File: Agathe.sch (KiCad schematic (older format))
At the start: 173 parts, among them J1 Conn_01x04_Female, J2 GPIO 1, J3 GPIO 2, J4 Conn_01x02_Female, SW1 SW_Push, U1 ATmega32U4-AU, U2 PRTR5V0U2X, Y1 Crystal_GND24_Small

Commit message: add value for rst resistor and crystal (#2)
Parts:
- R4: value R_Small -> 10k
- Y1: value Crystal_GND24_Small -> 16MHz
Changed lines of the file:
@@
 P 3950 7150
 F 0 "Y1" V 3904 7294 50  0000 L CNN
-F 1 "Crystal_GND24_Small" V 3995 7294 50  0000 L CNN
+F 1 "16MHz" V 3995 7294 50  0000 L CNN
 F 2 "Crystal:Crystal_SMD_3225-4Pin_3.2x2.5mm" H 3950 7150 50  0001 C CNN
 F 3 "~" H 3950 7150 50  0001 C CNN
@@
 P 1350 900
 F 0 "R4" H 1409 946 50  0000 L CNN
-F 1 "R_Small" H 1409 855 50  0000 L CNN
+F 1 "10k" H 1409 855 50  0000 L CNN
 F 2 "Resistor_SMD:R_0805_2012Metric" H 1350 900 50  0001 C CNN
 F 3 "~" H 1350 900 50  0001 C CNN

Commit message: Move J2 to top
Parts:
- removed J2: GPIO 1, Connector_PinHeader_2.54mm:PinHeader_1x01_P2.54mm_Vertical, symbol Connector:Conn_01x01_Female
- removed J3: GPIO 2, Connector_PinHeader_2.54mm:PinHeader_1x01_P2.54mm_Vertical, symbol Connector:Conn_01x01_Female
- added J2: Conn_01x02_Female, Connector_PinHeader_2.54mm:PinHeader_1x02_P2.54mm_Vertical, symbol Connector:Conn_01x02_Female
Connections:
- net labels added: GPIO1, GPIO2
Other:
- moved on the sheet: J4
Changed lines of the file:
@@
 Connection ~ 10000 3200
-$Comp
-L MCU_Microchip_ATmega:ATmega32U4-AU U1
-U 1 1 5EC4E28C
-P 1950 2700
-F 0 "U1" H 1950 811 50  0000 C CNN
-F 1 "ATmega32U4-AU" H 1950 720 50  0000 C CNN
-F 2 "Keebio-Parts:ATMEGA32U4-AU" H 1950 2700 50  0001 C CIN
-F 3 "http://ww1.microchip.com/downloads/en/DeviceDoc/Atmel-7766-8-bit-AVR-ATmega16U4-32U4_Datasheet.pdf" H 1950 2700 50  0001 C CNN
-	1    1950 2700
-	1    0    0    -1
-$EndComp
 $Comp
 L power:GND #PWR0101
@@
 Wire Wire Line
 	1950 4500 1850 4500
-Connection ~ 1950 4500
 $Comp
 L power:+5V #PWR0102
@@
 Wire Wire Line
 	1850 700  1850 900
-Wire Wire Line
-	1850 900  1950 900
-Connection ~ 1850 900
-Connection ~ 1950 900
-Wire Wire Line
-	1950 900  2050 900
 $Comp
 L Device:R_Small R1
@@
 Wire Wire Line
 	1350 1000 1350 1200
-Connection ~ 1350 1200
 $Comp
 L power:+5V #PWR0110
@@
 Text GLabel 2550 2400 2    50   Input ~ 0
 COL13
-Wire Wire Line
-	2550 3300 2900 3300
 Text GLabel 2550 2500 2    50   Input ~ 0
 COL12
@@
 $EndComp
 $Comp
-L Connector:Conn_01x01_Female J2
-U 1 1 5F7E232B
-P 2750 3400
-F 0 "J2" H 2778 3426 50  0000 L CNN
-F 1 "GPIO 1" H 2778 3335 50  0000 L CNN
-F 2 "Connector_PinHeader_2.54mm:PinHeader_1x01_P2.54mm_Vertical" H 2750 3400 50  0001 C CNN
-F 3 "~" H 2750 3400 50  0001 C CNN
-	1    2750 3400
-	1    0    0    -1
-$EndComp
-$Comp
-L Connector:Conn_01x01_Female J3
-U 1 1 5F7E3E80
-P 2750 4000
-F 0 "J3" H 2778 4026 50  0000 L CNN
-F 1 "GPIO 2" H 2778 3935 50  0000 L CNN
-F 2 "Connector_PinHeader_2.54mm:PinHeader_1x01_P2.54mm_Vertical" H 2750 4000 50  0001 C CNN
-F 3 "~" H 2750 4000 50  0001 C CNN
-	1    2750 4000
-	1    0    0    -1
-$EndComp
-$Comp
 L Connector:Conn_01x02_Female J4
 U 1 1 5F803717
-P 4850 6600
-F 0 "J4" H 4878 6576 50  0000 L CNN
-F 1 "Conn_01x02_Female" H 4878 6485 50  0000 L CNN
-F 2 "Connector_PinHeader_2.54mm:PinHeader_1x02_P2.54mm_Vertical" H 4850 6600 50  0001 C CNN
-F 3 "~" H 4850 6600 50  0001 C CNN
-	1    4850 6600
+P 5200 6450
+F 0 "J4" H 5228 6426 50  0000 L CNN
+F 1 "Conn_01x02_Female" H 5228 6335 50  0000 L CNN
+F 2 "Connector_PinHeader_2.54mm:PinHeader_1x02_P2.54mm_Vertical" H 5200 6450 50  0001 C CNN
+F 3 "~" H 5200 6450 50  0001 C CNN
+	1    5200 6450
 	1    0    0    -1
 $EndComp
@@
 L power:VCC #PWR03
 U 1 1 5F805F11
-P 4650 6600
-F 0 "#PWR03" H 4650 6450 50  0001 C CNN
-F 1 "VCC" H 4665 6773 50  0000 C CNN
-F 2 "" H 4650 6600 50  0001 C CNN
-F 3 "" H 4650 6600 50  0001 C CNN
-	1    4650 6600
+P 5000 6450
+F 0 "#PWR03" H 5000 6300 50  0001 C CNN
+F 1 "VCC" H 5015 6623 50  0000 C CNN
+F 2 "" H 5000 6450 50  0001 C CNN
+F 3 "" H 5000 6450 50  0001 C CNN
+	1    5000 6450
 	1    0    0    -1
 $EndComp
@@
 L power:GND #PWR04
 U 1 1 5F807ABA
-P 4650 6700
-F 0 "#PWR04" H 4650 6450 50  0001 C CNN
-F 1 "GND" H 4655 6527 50  0000 C CNN
-F 2 "" H 4650 6700 50  0001 C CNN
-F 3 "" H 4650 6700 50  0001 C CNN
-	1    4650 6700
-	1    0    0    -1
-$EndComp
+P 5000 6550
+F 0 "#PWR04" H 5000 6300 50  0001 C CNN
+F 1 "GND" H 5005 6377 50  0000 C CNN
+F 2 "" H 5000 6550 50  0001 C CNN
+F 3 "" H 5000 6550 50  0001 C CNN
+	1    5000 6550
+	1    0    0    -1
+$EndComp
+$Comp
+L Connector:Conn_01x02_Female J2
+U 1 1 5F858F30
+P 5150 7150
+F 0 "J2" H 5178 7126 50  0000 L CNN
+F 1 "Conn_01x02_Female" H 5178 7035 50  0000 L CNN
+F 2 "Connector_PinHeader_2.54mm:PinHeader_1x02_P2.54mm_Vertical" H 5150 7150 50  0001 C CNN
+F 3 "~" H 5150 7150 50  0001 C CNN
+	1    5150 7150
+	1    0    0    -1
+$EndComp
+Text GLabel 2550 4000 2    50   Input ~ 0
+GPIO2
+Connection ~ 1350 1200
+Connection ~ 1950 900
+Connection ~ 1850 900
+Wire Wire Line
+	1850 900  1950 900
+Connection ~ 1950 4500
+Wire Wire Line
+	2550 3300 2900 3300
+Wire Wire Line
+	1950 900  2050 900
+Text GLabel 2550 3400 2    50   Input ~ 0
+GPIO1
+$Comp
+L MCU_Microchip_ATmega:ATmega32U4-AU U1
+U 1 1 5EC4E28C
+P 1950 2700
+F 0 "U1" H 1950 811 50  0000 C CNN
+F 1 "ATmega32U4-AU" H 1950 720 50  0000 C CNN
+F 2 "Keebio-Parts:ATMEGA32U4-AU" H 1950 2700 50  0001 C CIN
+F 3 "http://ww1.microchip.com/downloads/en/DeviceDoc/Atmel-7766-8-bit-AVR-ATmega16U4-32U4_Datasheet.pdf" H 1950 2700 50  0001 C CNN
+	1    1950 2700
+	1    0    0    -1
+$EndComp
+Text GLabel 4950 7150 0    50   Input ~ 0
+GPIO1
+Text GLabel 4950 7250 0    50   Input ~ 0
+GPIO2
 $EndSCHEMATC

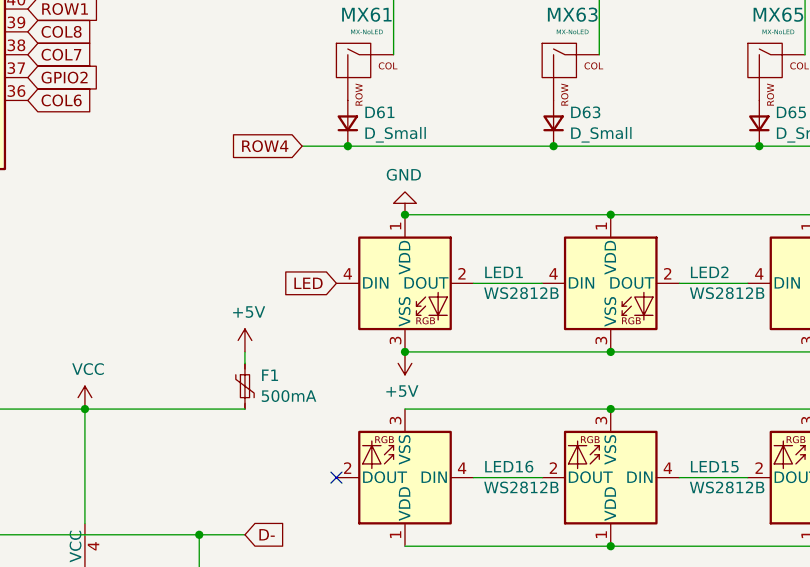
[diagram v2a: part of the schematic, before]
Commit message: reverse vcc and gnd on leds (#9)
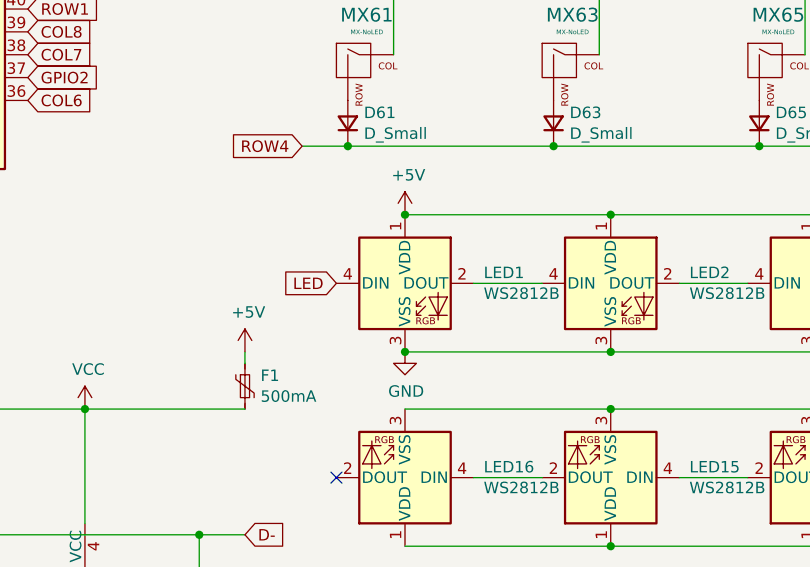
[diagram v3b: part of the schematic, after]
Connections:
- net +5V: now also LED1.1 (VDD), LED10.1 (VDD), LED11.1 (VDD), LED12.1 (VDD), LED13.1 (VDD), LED14.1 (VDD), LED15.1 (VDD), LED16.1 (VDD), LED2.1 (VDD), LED3.1 (VDD), LED4.1 (VDD), LED5.1 (VDD), LED6.1 (VDD), LED7.1 (VDD), LED8.1 (VDD), LED9.1 (VDD); no longer LED1.3 (VSS), LED10.3 (VSS), LED11.3 (VSS), LED12.3 (VSS), LED13.3 (VSS), LED14.3 (VSS), LED15.3 (VSS), LED16.3 (VSS), LED2.3 (VSS), LED3.3 (VSS), LED4.3 (VSS), LED5.3 (VSS), LED6.3 (VSS), LED7.3 (VSS), LED8.3 (VSS), LED9.3 (VSS)
- net GND: now also LED1.3 (VSS), LED10.3 (VSS), LED11.3 (VSS), LED12.3 (VSS), LED13.3 (VSS), LED14.3 (VSS), LED15.3 (VSS), LED16.3 (VSS), LED2.3 (VSS), LED3.3 (VSS), LED4.3 (VSS), LED5.3 (VSS), LED6.3 (VSS), LED7.3 (VSS), LED8.3 (VSS), LED9.3 (VSS); no longer LED1.1 (VDD), LED10.1 (VDD), LED11.1 (VDD), LED12.1 (VDD), LED13.1 (VDD), LED14.1 (VDD), LED15.1 (VDD), LED16.1 (VDD), LED2.1 (VDD), LED3.1 (VDD), LED4.1 (VDD), LED5.1 (VDD), LED6.1 (VDD), LED7.1 (VDD), LED8.1 (VDD), LED9.1 (VDD)
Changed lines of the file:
@@
 L power:GND #PWR0117
 U 1 1 5EE29498
-P 4200 4600
-F 0 "#PWR0117" H 4200 4350 50  0001 C CNN
-F 1 "GND" H 4205 4427 50  0000 C CNN
-F 2 "" H 4200 4600 50  0001 C CNN
-F 3 "" H 4200 4600 50  0001 C CNN
-	1    4200 4600
-	-1   0    0    1
+P 4200 5200
+F 0 "#PWR0117" H 4200 4950 50  0001 C CNN
+F 1 "GND" H 4205 5027 50  0000 C CNN
+F 2 "" H 4200 5200 50  0001 C CNN
+F 3 "" H 4200 5200 50  0001 C CNN
+	1    4200 5200
+	1    0    0    -1
 $EndComp
 Text GLabel 3900 4900 0    50   Input ~ 0
@@
 L power:+5V #PWR0118
 U 1 1 5F100FF1
-P 4200 5200
-F 0 "#PWR0118" H 4200 5050 50  0001 C CNN
-F 1 "+5V" H 4215 5373 50  0000 C CNN
-F 2 "" H 4200 5200 50  0001 C CNN
-F 3 "" H 4200 5200 50  0001 C CNN
-	1    4200 5200
-	-1   0    0    1
+P 4200 4600
+F 0 "#PWR0118" H 4200 4450 50  0001 C CNN
+F 1 "+5V" H 4215 4773 50  0000 C CNN
+F 2 "" H 4200 4600 50  0001 C CNN
+F 3 "" H 4200 4600 50  0001 C CNN
+	1    4200 4600
+	1    0    0    -1
 $EndComp
 Connection ~ 4200 5200

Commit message: add a capacitor
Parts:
- added C8: 0.1uF, Capacitor_SMD:C_0805_2012Metric, symbol Device:C_Small
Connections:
- net +5V: now also C8.1
- net GND: now also C8.2
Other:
- moved on the sheet: C5
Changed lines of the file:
@@
 L Device:C_Small C5
 U 1 1 5ED00BF8
-P 1800 7450
-F 0 "C5" H 1892 7496 50  0000 L CNN
-F 1 "10uF" H 1892 7405 50  0000 L CNN
-F 2 "Capacitor_SMD:C_0805_2012Metric" H 1800 7450 50  0001 C CNN
-F 3 "~" H 1800 7450 50  0001 C CNN
-	1    1800 7450
+P 2200 7450
+F 0 "C5" H 2292 7496 50  0000 L CNN
+F 1 "10uF" H 2292 7405 50  0000 L CNN
+F 2 "Capacitor_SMD:C_0805_2012Metric" H 2200 7450 50  0001 C CNN
+F 3 "~" H 2200 7450 50  0001 C CNN
+	1    2200 7450
 	1    0    0    -1
 $EndComp
@@
 L power:+5V #PWR0105
 U 1 1 5ED02584
-P 1250 7350
-F 0 "#PWR0105" H 1250 7200 50  0001 C CNN
-F 1 "+5V" H 1265 7523 50  0000 C CNN
-F 2 "" H 1250 7350 50  0001 C CNN
-F 3 "" H 1250 7350 50  0001 C CNN
-	1    1250 7350
+P 1400 7350
+F 0 "#PWR0105" H 1400 7200 50  0001 C CNN
+F 1 "+5V" H 1415 7523 50  0000 C CNN
+F 2 "" H 1400 7350 50  0001 C CNN
+F 3 "" H 1400 7350 50  0001 C CNN
+	1    1400 7350
 	1    0    0    -1
 $EndComp
@@
 L power:GND #PWR0106
 U 1 1 5ED03888
-P 1250 7550
-F 0 "#PWR0106" H 1250 7300 50  0001 C CNN
-F 1 "GND" H 1255 7377 50  0000 C CNN
-F 2 "" H 1250 7550 50  0001 C CNN
-F 3 "" H 1250 7550 50  0001 C CNN
-	1    1250 7550
-	1    0    0    -1
-$EndComp
-Connection ~ 1250 7550
-Wire Wire Line
-	1800 7350 1400 7350
+P 1400 7550
+F 0 "#PWR0106" H 1400 7300 50  0001 C CNN
+F 1 "GND" H 1405 7377 50  0000 C CNN
+F 2 "" H 1400 7550 50  0001 C CNN
+F 3 "" H 1400 7550 50  0001 C CNN
+	1    1400 7550
+	1    0    0    -1
+$EndComp
 Connection ~ 1000 7350
 Wire Wire Line
 	1000 7350 600  7350
-Connection ~ 1250 7350
-Wire Wire Line
-	1250 7350 1000 7350
 Connection ~ 1400 7350
-Wire Wire Line
-	1400 7350 1250 7350
 $Comp
 L power:+5V #PWR0107
@@
 Wire Wire Line
 	600  7550 1000 7550
-Wire Wire Line
-	1250 7550 1400 7550
 Connection ~ 1000 7550
-Wire Wire Line
-	1000 7550 1250 7550
 Connection ~ 1400 7550
-Wire Wire Line
-	1400 7550 1800 7550
 NoConn ~ 1550 6550
 Wire Wire Line
@@
 Text GLabel 4950 7250 0    50   Input ~ 0
 GPIO2
+$Comp
+L Device:C_Small C8
+U 1 1 5F97460A
+P 1800 7450
+F 0 "C8" H 1892 7496 50  0000 L CNN
+F 1 "0.1uF" H 1892 7405 50  0000 L CNN
+F 2 "Capacitor_SMD:C_0805_2012Metric" H 1800 7450 50  0001 C CNN
+F 3 "~" H 1800 7450 50  0001 C CNN
+	1    1800 7450
+	1    0    0    -1
+$EndComp
+Wire Wire Line
+	1400 7350 1800 7350
+Wire Wire Line
+	1400 7550 1800 7550
+Wire Wire Line
+	1800 7550 2200 7550
+Connection ~ 1800 7550
+Wire Wire Line
+	1800 7350 2200 7350
+Connection ~ 1800 7350
+Wire Wire Line
+	1000 7550 1400 7550
+Wire Wire Line
+	1000 7350 1400 7350
 $EndSCHEMATC

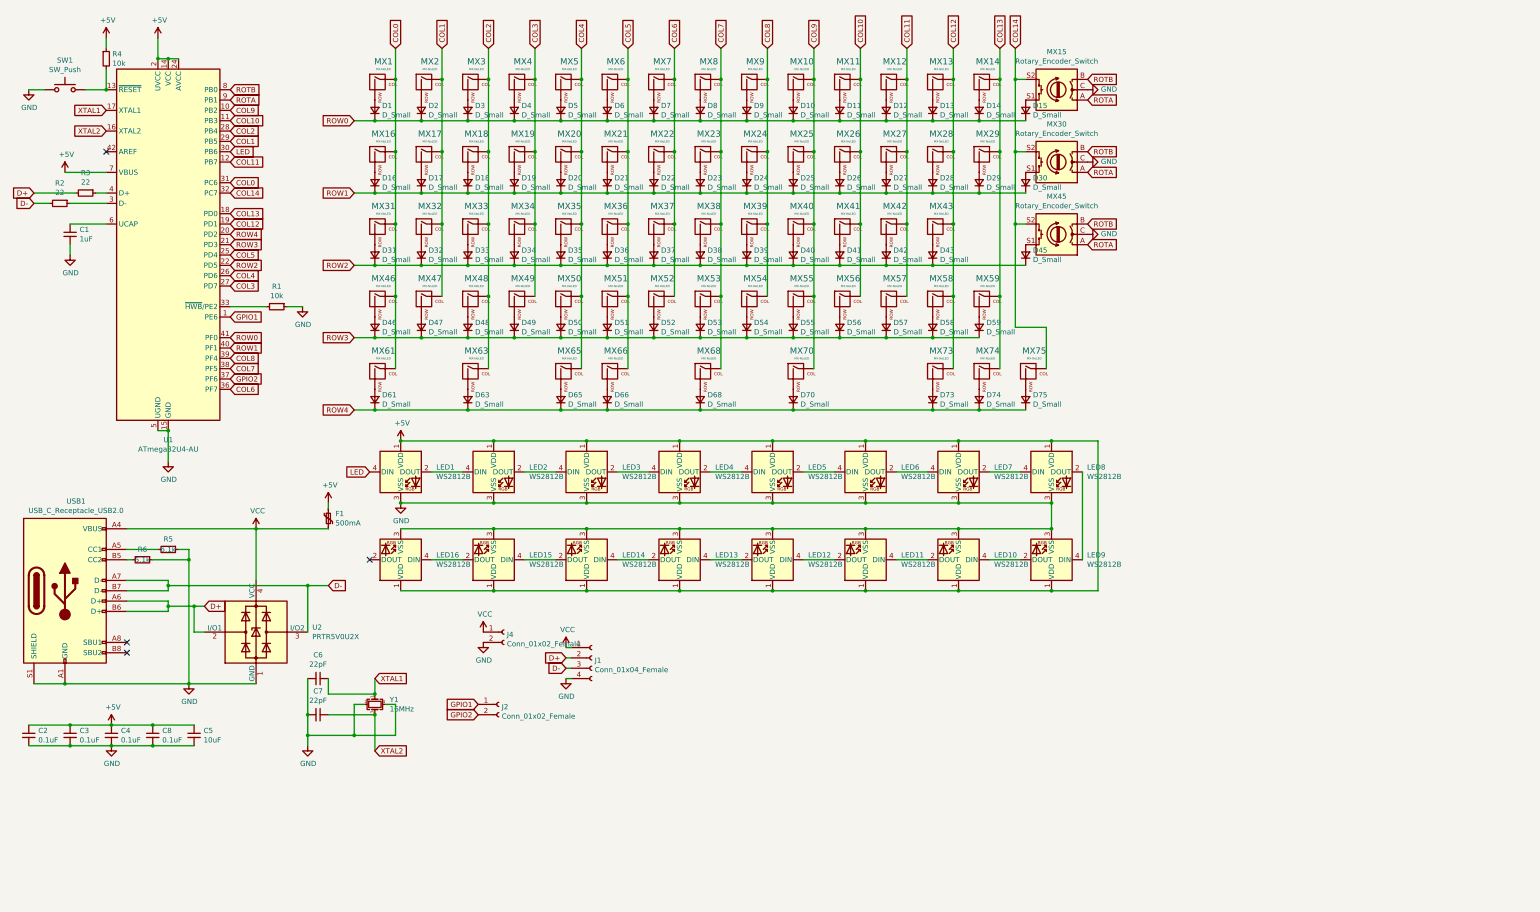
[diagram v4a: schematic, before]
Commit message: update shematics
add spi interface
add 6 leds
change the esp
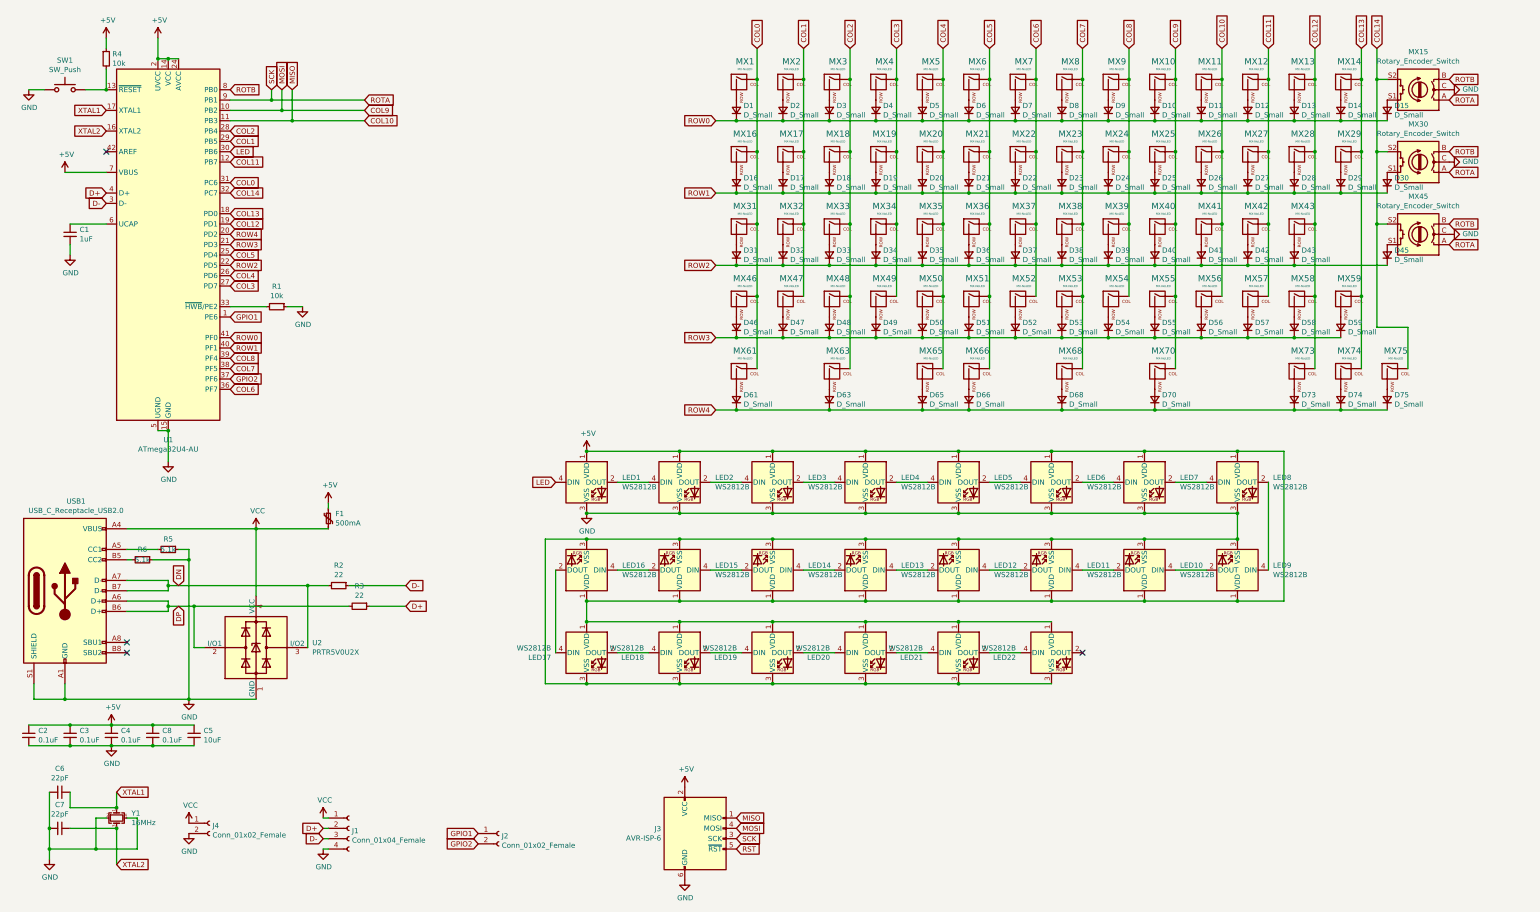
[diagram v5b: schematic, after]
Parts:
- added J3: AVR-ISP-6, random-keyboard-parts:Reset_Pretty-Mask, symbol Connector:AVR-ISP-6
- added LED17, LED18, LED19, LED20, LED21, LED22: WS2812B, LED_SMD:LED_WS2812B_PLCC4_5.0x5.0mm_P3.2mm, symbol LED:WS2812B
- U2: footprint Package_TO_SOT_SMD:SOT-143 -> random-keyboard-parts:SOT143B
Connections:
- net +5V: now also J3.2 (VCC), LED17.1 (VDD), LED18.1 (VDD), LED19.1 (VDD), LED20.1 (VDD), LED21.1 (VDD), LED22.1 (VDD)
- net COL10: now also J3.1 (MISO)
- net COL9: now also J3.4 (MOSI)
- net D+: now also R3.1, U1.4 (D+); no longer R3.2, U2.2 (I/O1), USB1.A6 (D+), USB1.B6 (D+)
- net D-: now also R2.1, U1.3 (D-); no longer R2.2, U2.3 (I/O2), USB1.A7 (D-), USB1.B7 (D-)
- net GND: now also J3.6 (GND), LED17.3 (VSS), LED18.3 (VSS), LED19.3 (VSS), LED20.3 (VSS), LED21.3 (VSS), LED22.3 (VSS)
- net ROTA: now also J3.3 (SCK)
- net at LED16.2 (DOUT): now also LED17.4 (DIN)
- new net: LED17.2 (DOUT), LED18.4 (DIN)
- new net: LED18.2 (DOUT), LED19.4 (DIN)
- new net: LED19.2 (DOUT), LED20.4 (DIN)
- new net: LED20.2 (DOUT), LED21.4 (DIN)
- new net: LED21.2 (DOUT), LED22.4 (DIN)
- new net DN: R2.2, U2.3 (I/O2), USB1.A7 (D-), USB1.B7 (D-)
- new net DP: R3.2, U2.2 (I/O1), USB1.A6 (D+), USB1.B6 (D+)
- new net RST: J3.5 (~RST)
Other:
- moved on the sheet: C6, C7, D1, D10, D11, D12, D13, D14, D15, D16, D17, D18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

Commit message: j'ai putain de tout refait putain
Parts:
- removed J2, J4: Conn_01x02_Female, Connector_PinHeader_2.54mm:PinHeader_1x02_P2.54mm_Vertical, symbol Connector:Conn_01x02_Female
- removed LED17, LED18, LED19, LED20, LED21, LED22: WS2812B, LED_SMD:LED_WS2812B_PLCC4_5.0x5.0mm_P3.2mm, symbol LED:WS2812B
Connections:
- net GPIO1 is gone; now on net ROW0: U1.1 (PE6)
- net GPIO2 is gone; now on net COL5: U1.37 (PF6)
- net COL0: now also U1.29 (PB5); no longer U1.31 (PC6)
- net COL1: now also U1.30 (PB6); no longer U1.29 (PB5)
- net COL10: now also U1.22 (PD5); no longer J3.1 (MISO), U1.11 (PB3)
- net COL11: now also U1.25 (PD4); no longer U1.12 (PB7)
- net COL12: now also U1.26 (PD6); no longer U1.19 (PD1)
- net COL13: now also U1.27 (PD7); no longer U1.18 (PD0)
- net COL14: now also U1.28 (PB4); no longer U1.32 (PC7)
- net COL2: now also U1.31 (PC6); no longer U1.28 (PB4)
- net COL3: now also U1.32 (PC7); no longer U1.27 (PD7)
- net COL4: now also U1.36 (PF7); no longer U1.26 (PD6)
- net COL5: no longer U1.25 (PD4)
- net COL6: now also U1.18 (PD0); no longer U1.36 (PF7)
- net COL7: now also U1.19 (PD1); no longer U1.38 (PF5)
- net COL8: now also U1.20 (PD2); no longer U1.39 (PF4)
- net COL9: now also U1.21 (PD3); no longer J3.4 (MOSI), U1.10 (PB2)
- net D+: no longer J1.2 (Pin_2)
- net D-: no longer J1.3 (Pin_3)
- net DN: now also J1.3 (Pin_3)
- net DP: now also J1.2 (Pin_2)
- net LED: now also U1.8 (PB0); no longer U1.30 (PB6)
- net ROTB: now also U1.12 (PB7); no longer U1.8 (PB0)
- net ROW0: no longer U1.41 (PF0)
- net ROW1: now also U1.41 (PF0); no longer U1.40 (PF1)
- net ROW2: now also U1.40 (PF1); no longer U1.22 (PD5)
- net ROW3: now also U1.39 (PF4); no longer U1.21 (PD3)
- net ROW4: now also U1.38 (PF5); no longer U1.20 (PD2)
- net RST: now also R4.2, SW1.2, U1.13 (~RESET)
- net ROTA renamed MISO
- net MISO: now also J3.1 (MISO), U1.11 (PB3); no longer J3.3 (SCK), U1.9 (PB1)
- new net MOSI: J3.4 (MOSI), U1.10 (PB2)
- new net SCK: J3.3 (SCK), U1.9 (PB1)
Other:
- moved on the sheet: J1, J3, R4, SW1

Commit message: add some stuff after a review from @plut0nium
Some new feature from the @masterzen blog article
http://www.masterzen.fr/2020/10/20/designing-a-keyboard-part3/
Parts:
- added C10, C11, C9: 0.1uF, Capacitor_SMD:C_0805_2012Metric, symbol Device:C_Small
- added FB1: Ferrite_Bead_Small, Inductor_SMD:L_0805_2012Metric_Pad1.15x1.40mm_HandSolder, symbol Device:Ferrite_Bead_Small
- added R7: 350, Resistor_SMD:R_0805_2012Metric, symbol Device:R_Small
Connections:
- net +5V: now also C10.1, C11.1, C9.2
- net GND: now also J1.1 (Pin_1), C10.2, C11.2, C9.1, FB1.1; no longer J1.4 (Pin_4), USB1.S1 (SHIELD)
- net LED: now also R7.2; no longer LED1.4 (DIN)
- net VCC: now also J1.4 (Pin_4); no longer J1.1 (Pin_1)
- new net: LED1.4 (DIN), R7.1
- new net Earth: FB1.2, USB1.S1 (SHIELD)
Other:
- moved on the sheet: LED1, LED13, LED14, LED15, LED16, LED2, LED3, LED4
